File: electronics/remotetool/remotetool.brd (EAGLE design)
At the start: 127 x 99.1 mm, 48 parts

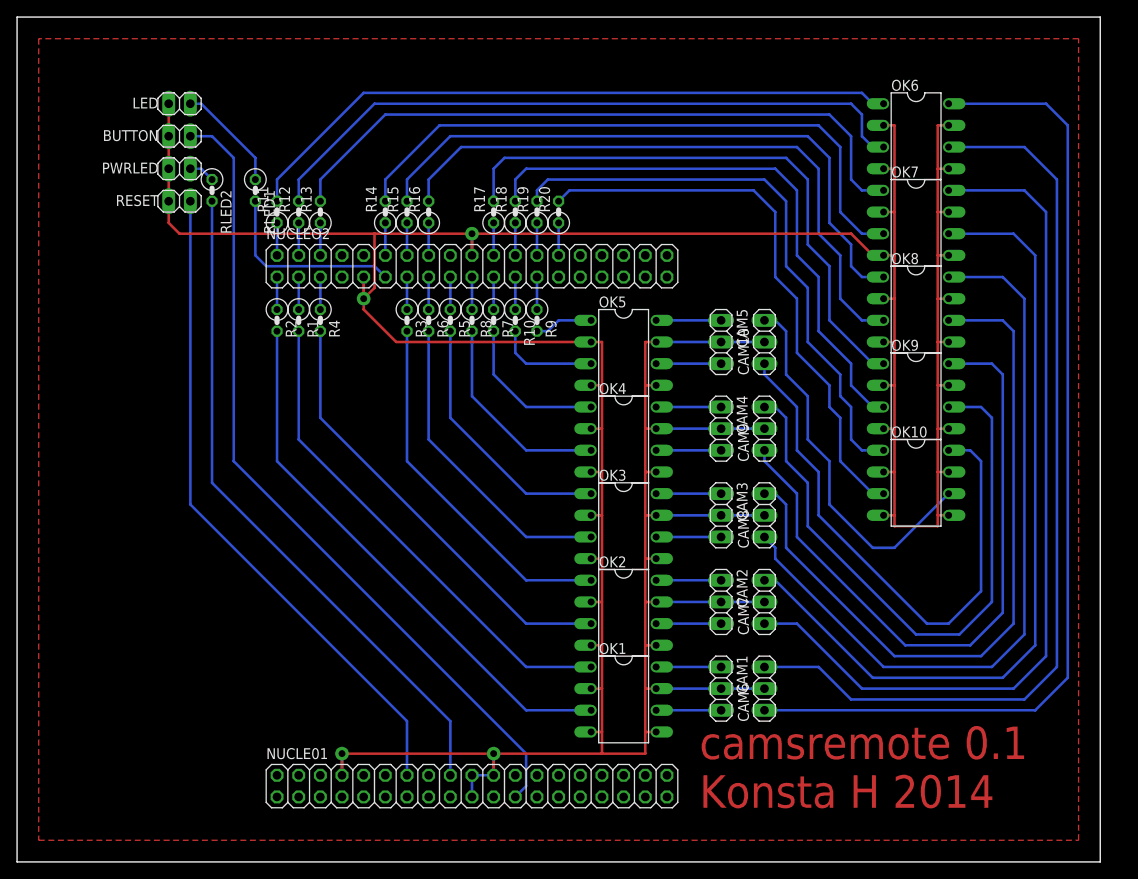
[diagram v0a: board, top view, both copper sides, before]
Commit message: remotetool: simplify ground signals
- rearrange ground signals a bit, remove most top layer traces
- make it possible to route in a single layer, add ground polygon to
  bottom layer too
- leave some vias for top ground plane
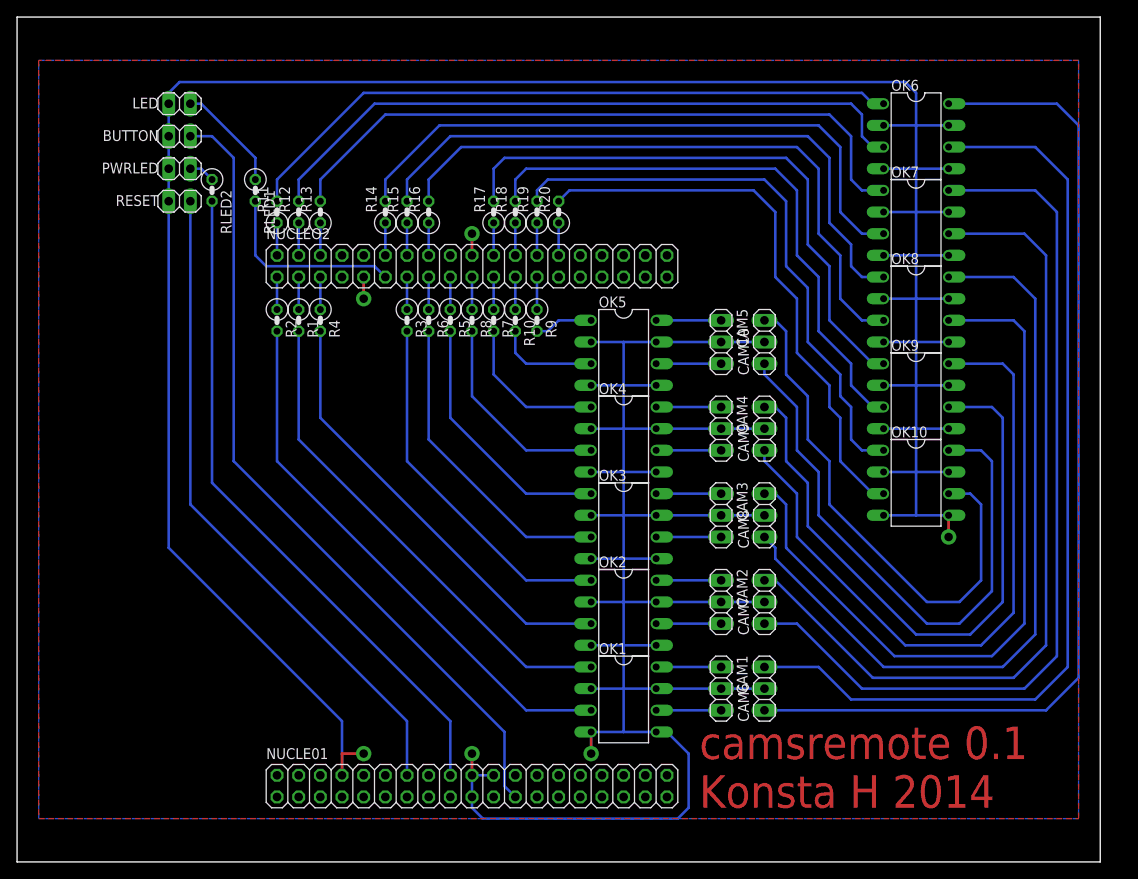
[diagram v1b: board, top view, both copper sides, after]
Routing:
- net GND: track 507.9 -> 565.3 mm, vias 4 -> 6
- net N$40: track 44.2 -> 62.3 mm
- net N$35: track 77.5 -> 80.1 mm
- net N$27: track 102.3 -> 104.8 mm
- net N$39: track 65.9 -> 68.4 mm
- net N$36: track 72.4 -> 75.0 mm
- net N$32: track 84.1 -> 86.6 mm
- net N$31: track 88.4 -> 91.0 mm
- net N$28: track 95.0 -> 97.5 mm
- net N$24: track 108.9 -> 111.4 mm
- net N$23: track 116.9 -> 119.5 mm
- net N$42: track 95.8 -> 94.7 mm
- added copper zone on layer 16, net GND

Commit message: remotetool: rename second half as it should be
The second half of connectors is kind of mirrored from the optocoupler
point of view; rename signals so that all connectors are facing the same
way when installing. Also make the borrom row labels readable.
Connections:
- net FOCUS10: now also NUCLEO2.28, R20.1; no longer NUCLEO2.26, R19.1
- net FOCUS6: now also NUCLEO2.4, R12.1; no longer NUCLEO2.2, R11.1
- net FOCUS7: now also NUCLEO2.12, R14.1; no longer NUCLEO2.6, R13.1
- net FOCUS8: now also NUCLEO2.16, R16.1; no longer NUCLEO2.14, R15.1
- net FOCUS9: now also NUCLEO2.24, R18.1; no longer NUCLEO2.22, R17.1
- net SHUTTER10: now also NUCLEO2.26, R19.1; no longer NUCLEO2.28, R20.1
- net SHUTTER6: now also NUCLEO2.2, R11.1; no longer NUCLEO2.4, R12.1
- net SHUTTER7: now also NUCLEO2.6, R13.1; no longer NUCLEO2.12, R14.1
- net SHUTTER8: now also NUCLEO2.14, R15.1; no longer NUCLEO2.16, R16.1
- net SHUTTER9: now also NUCLEO2.22, R17.1; no longer NUCLEO2.24, R18.1
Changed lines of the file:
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@@
 <element name="R11" library="resistor" package="0207/2V" value="" x="20.32" y="68.58" rot="R90"/>
 <element name="R12" library="resistor" package="0207/2V" value="" x="22.86" y="68.58" rot="R90"/>
-<element name="CAM6" library="pinhead" package="1X03" value="" x="77.47" y="12.7" rot="R90"/>
+<element name="CAM6" library="pinhead" package="1X03" value="" x="77.47" y="12.7" smashed="yes" rot="R90">
+<attribute name="NAME" x="80.7212" y="8.8138" size="1.27" layer="25" ratio="10" rot="R90"/>
+<attribute name="VALUE" x="80.645" y="8.89" size="1.27" layer="27" rot="R90"/>
+</element>
 <element name="OK7" library="optocoupler" package="DIL08" value="ILD621" x="95.25" y="67.31" rot="R270">
 <attribute name="OC_NEWARK" value="58K1678" x="91.44" y="105.41" size="1.778" layer="27" rot="R270" display="off"/>
@@
 <element name="R13" library="resistor" package="0207/2V" value="" x="25.4" y="68.58" rot="R90"/>
 <element name="R14" library="resistor" package="0207/2V" value="" x="33.02" y="68.58" rot="R90"/>
-<element name="CAM7" library="pinhead" package="1X03" value="" x="77.47" y="22.86" rot="R90"/>
+<element name="CAM7" library="pinhead" package="1X03" value="" x="77.47" y="22.86" smashed="yes" rot="R90">
+<attribute name="NAME" x="80.7212" y="18.9738" size="1.27" layer="25" ratio="10" rot="R90"/>
+<attribute name="VALUE" x="80.645" y="19.05" size="1.27" layer="27" rot="R90"/>
+</element>
 <element name="OK8" library="optocoupler" package="DIL08" value="ILD621" x="95.25" y="57.15" rot="R270">
 <attribute name="OC_NEWARK" value="58K1678" x="74.93" y="120.65" size="1.778" layer="27" rot="R270" display="off"/>
@@
 <element name="R15" library="resistor" package="0207/2V" value="" x="35.56" y="68.58" rot="R90"/>
 <element name="R16" library="resistor" package="0207/2V" value="" x="38.1" y="68.58" rot="R90"/>
-<element name="CAM8" library="pinhead" package="1X03" value="" x="77.47" y="33.02" rot="R90"/>
+<element name="CAM8" library="pinhead" package="1X03" value="" x="77.47" y="33.02" smashed="yes" rot="R90">
+<attribute name="NAME" x="80.7212" y="29.1338" size="1.27" layer="25" ratio="10" rot="R90"/>
+<attribute name="VALUE" x="80.645" y="29.21" size="1.27" layer="27" rot="R90"/>
+</element>
 <element name="OK9" library="optocoupler" package="DIL08" value="ILD621" x="95.25" y="46.99" rot="R270">
 <attribute name="OC_NEWARK" value="58K1678" x="110.49" y="59.69" size="1.778" layer="27" rot="R270" display="off"/>
@@
 <element name="R17" library="resistor" package="0207/2V" value="" x="45.72" y="68.58" rot="R90"/>
 <element name="R18" library="resistor" package="0207/2V" value="" x="48.26" y="68.58" rot="R90"/>
-<element name="CAM9" library="pinhead" package="1X03" value="" x="77.47" y="43.18" rot="R90"/>
+<element name="CAM9" library="pinhead" package="1X03" value="" x="77.47" y="43.18" smashed="yes" rot="R90">
+<attribute name="NAME" x="80.7212" y="39.2938" size="1.27" layer="25" ratio="10" rot="R90"/>
+<attribute name="VALUE" x="80.645" y="39.37" size="1.27" layer="27" rot="R90"/>
+</element>
 <element name="OK10" library="optocoupler" package="DIL08" value="ILD621" x="95.25" y="36.83" rot="R270">
 <attribute name="OC_NEWARK" value="58K1678" x="93.98" y="74.93" size="1.778" layer="27" rot="R270" display="off"/>
@@
 <element name="R19" library="resistor" package="0207/2V" value="" x="50.8" y="68.58" rot="R90"/>
 <element name="R20" library="resistor" package="0207/2V" value="" x="53.34" y="68.58" rot="R90"/>
-<element name="CAM10" library="pinhead" package="1X03" value="" x="77.47" y="53.34" rot="R90"/>
+<element name="CAM10" library="pinhead" package="1X03" value="" x="77.47" y="53.34" smashed="yes" rot="R90">
+<attribute name="NAME" x="80.7212" y="49.4538" size="1.27" layer="25" ratio="10" rot="R90"/>
+<attribute name="VALUE" x="80.645" y="49.53" size="1.27" layer="27" rot="R90"/>
+</element>
 <element name="LED" library="pinhead" package="1X02" value="" x="8.89" y="81.28" smashed="yes" rot="R180">
 <attribute name="NAME" x="6.4262" y="81.9912" size="1.27" layer="25" ratio="10" rot="R180"/>
@@
 <wire x1="43.18" y1="57.15" x2="43.18" y2="60.96" width="0.3048" layer="16"/>
 </signal>
-<signal name="SHUTTER6">
+<signal name="FOCUS6">
 <contactref element="R12" pad="1"/>
 <contactref element="NUCLEO2" pad="4"/>
 <wire x1="22.86" y1="67.31" x2="22.86" y2="63.5" width="0.3048" layer="16"/>
 </signal>
-<signal name="FOCUS6">
+<signal name="SHUTTER6">
 <contactref element="R11" pad="1"/>
 <contactref element="NUCLEO2" pad="2"/>
-<wire x1="20.32" y1="63.5" x2="20.32" y2="67.31" width="0.3048" layer="16"/>
-</signal>
-<signal name="SHUTTER8">
+<wire x1="20.32" y1="67.31" x2="20.32" y2="63.5" width="0.3048" layer="16"/>
+</signal>
+<signal name="FOCUS8">
 <contactref element="R16" pad="1"/>
 <contactref element="NUCLEO2" pad="16"/>
 <wire x1="38.1" y1="67.31" x2="38.1" y2="63.5" width="0.3048" layer="16"/>
 </signal>
-<signal name="FOCUS8">
+<signal name="SHUTTER8">
 <contactref element="R15" pad="1"/>
 <contactref element="NUCLEO2" pad="14"/>
-<wire x1="35.56" y1="63.5" x2="35.56" y2="67.31" width="0.3048" layer="16"/>
+<wire x1="35.56" y1="67.31" x2="35.56" y2="63.5" width="0.3048" layer="16"/>
 </signal>
 <signal name="FOCUS10">
-<contactref element="R19" pad="1"/>
-<contactref element="NUCLEO2" pad="26"/>
-<wire x1="50.8" y1="67.31" x2="50.8" y2="63.5" width="0.3048" layer="16"/>
-</signal>
-<signal name="SHUTTER10">
 <contactref element="R20" pad="1"/>
 <contactref element="NUCLEO2" pad="28"/>
-<wire x1="53.34" y1="63.5" x2="53.34" y2="67.31" width="0.3048" layer="16"/>
-</signal>
-<signal name="SHUTTER9">
+<wire x1="53.34" y1="67.31" x2="53.34" y2="63.5" width="0.3048" layer="16"/>
+</signal>
+<signal name="FOCUS9">
 <contactref element="R18" pad="1"/>
 <contactref element="NUCLEO2" pad="24"/>
-<wire x1="48.26" y1="63.5" x2="48.26" y2="67.31" width="0.3048" layer="16"/>
-</signal>
-<signal name="FOCUS9">
+<wire x1="48.26" y1="67.31" x2="48.26" y2="63.5" width="0.3048" layer="16"/>
+</signal>
+<signal name="SHUTTER9">
 <contactref element="R17" pad="1"/>
 <contactref element="NUCLEO2" pad="22"/>
 <wire x1="45.72" y1="67.31" x2="45.72" y2="63.5" width="0.3048" layer="16"/>
 </signal>
-<signal name="SHUTTER7">
+<signal name="FOCUS7">
 <contactref element="R14" pad="1"/>
 <contactref element="NUCLEO2" pad="12"/>
 <wire x1="33.02" y1="67.31" x2="33.02" y2="63.5" width="0.3048" layer="16"/>
 </signal>
-<signal name="FOCUS7">
+<signal name="SHUTTER7">
 <contactref element="R13" pad="1"/>
 <contactref element="NUCLEO2" pad="6"/>
@@
 <wire x1="11.43" y1="73.66" x2="10.16" y2="73.66" width="0.3048" layer="16"/>
 </signal>
+<signal name="SHUTTER10">
+<contactref element="R19" pad="1"/>
+<contactref element="NUCLEO2" pad="26"/>
+<wire x1="50.8" y1="67.31" x2="50.8" y2="63.5" width="0.3048" layer="16"/>
+</signal>
 </signals>
